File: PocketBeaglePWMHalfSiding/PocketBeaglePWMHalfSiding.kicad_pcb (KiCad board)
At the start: 2 copper layers, 149.9 x 128.3 mm, 61 parts, among them IC1 MCT6H, IC2 MCT6H, J1 RJ45, J2 RJ45, P1 POCKETBEAGLE-P1, P2 POCKETBEAGLE-P2, P3 C A0 A1 A2 A3 A4 A5 A6 A7, P4 C B0 B1 B2 B3 B4 B5 B6 B7, T1 + 15 in -, T2 + 15 out -, T3 In Track1 Out, T4 In Track1 Out, T5 Motor 1, T6 Motor 2, U1 TCAN332DR, U2 SN65HVD233-HT, U3 LM2574N-5.0, U4 PCA9685, U5 TBD62X83A, U6 TBD62X83A, U7 TC4428, U8 TC4428, U9 74HCT00

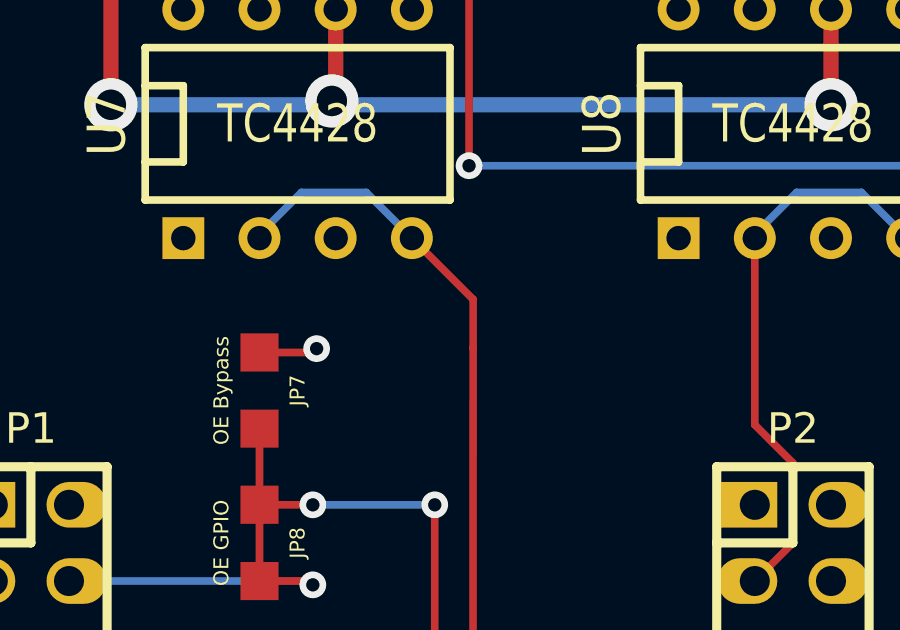
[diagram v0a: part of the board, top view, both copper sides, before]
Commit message: Mark orientation of ESP32 and PocketBeagle modules on the silk.
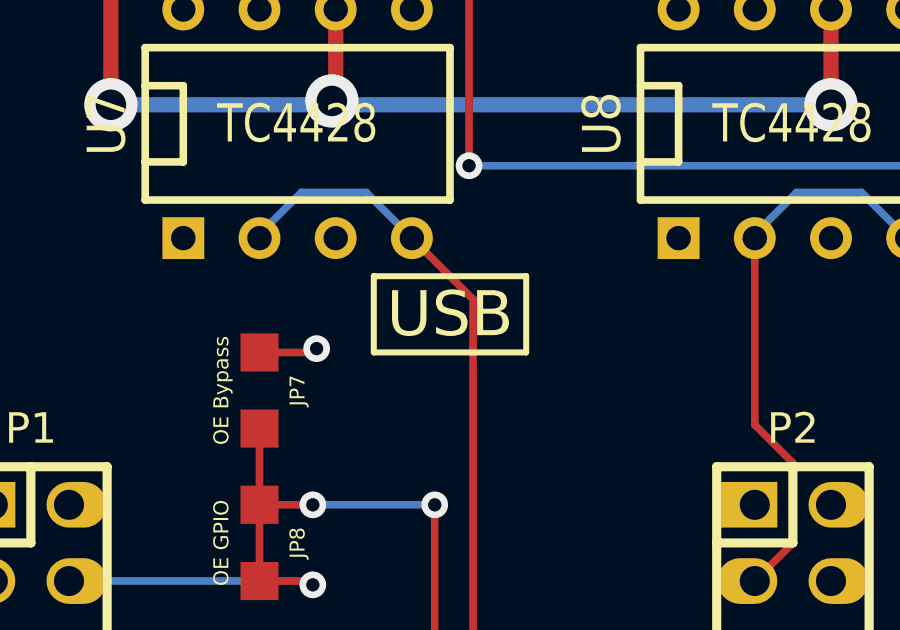
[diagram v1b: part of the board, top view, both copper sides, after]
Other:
- board text added: "USB"
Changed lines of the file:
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@@
     (area 38.269994 56.34548 243.868126 186.32358)
     (thickness 1.6)
-    (drawings 8)
+    (drawings 13)
     (tracks 644)
     (zones 0)
@@
     )
   )
+  (gr_line (start 144.78 73.66) (end 144.78 76.2) (angle 90) (layer F.SilkS) (width 0.2))
+  (gr_line (start 139.7 73.66) (end 144.78 73.66) (angle 90) (layer F.SilkS) (width 0.2))
+  (gr_line (start 139.7 76.2) (end 139.7 73.66) (angle 90) (layer F.SilkS) (width 0.2))
+  (gr_line (start 144.78 76.2) (end 139.7 76.2) (angle 90) (layer F.SilkS) (width 0.2))
+  (gr_text USB (at 142.24 74.93) (layer F.SilkS)
+    (effects (font (size 1.5 1.5) (thickness 0.3)))
+  )
   (gr_line (start 215.9 129.54) (end 163.83 129.54) (angle 90) (layer Edge.Cuts) (width 0.1))

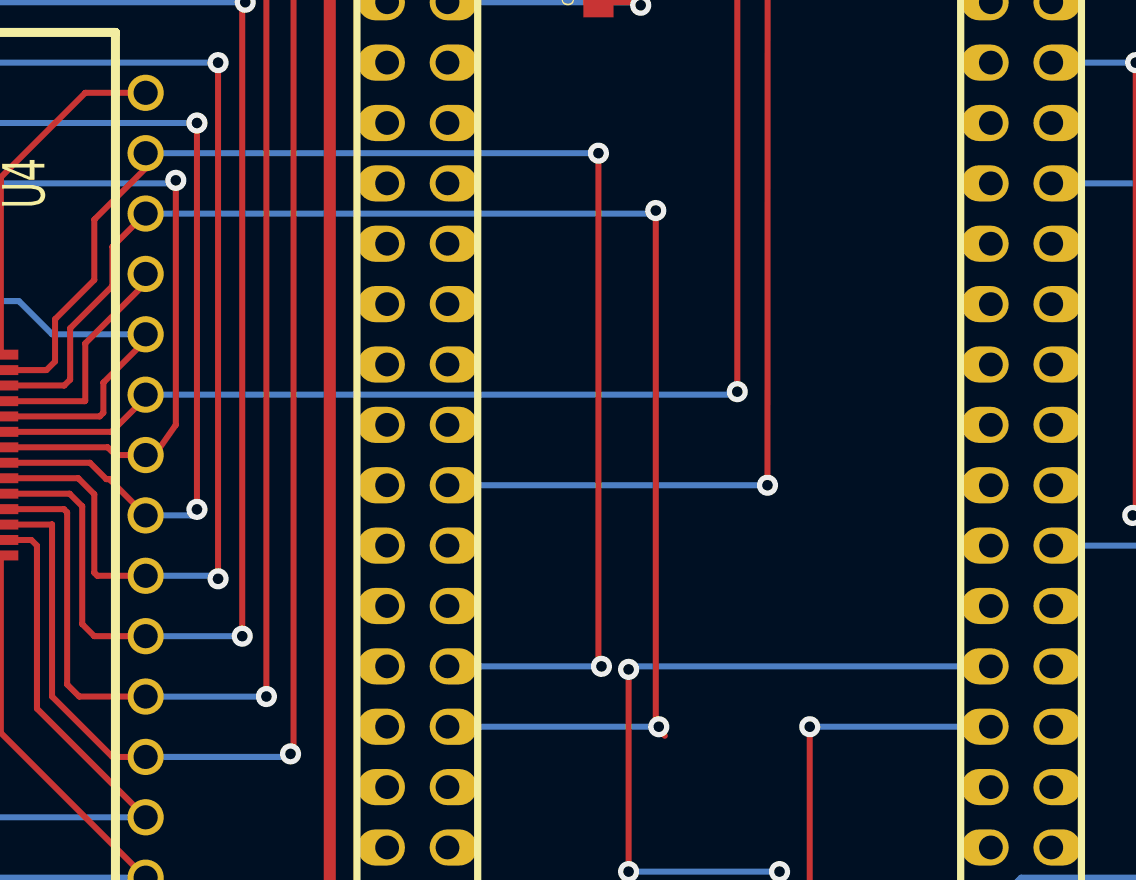
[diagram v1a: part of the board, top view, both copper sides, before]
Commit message: Move Pocket Beagle SDA usage from I2C2 to I2C1 (reserved I2C for eeprom?).
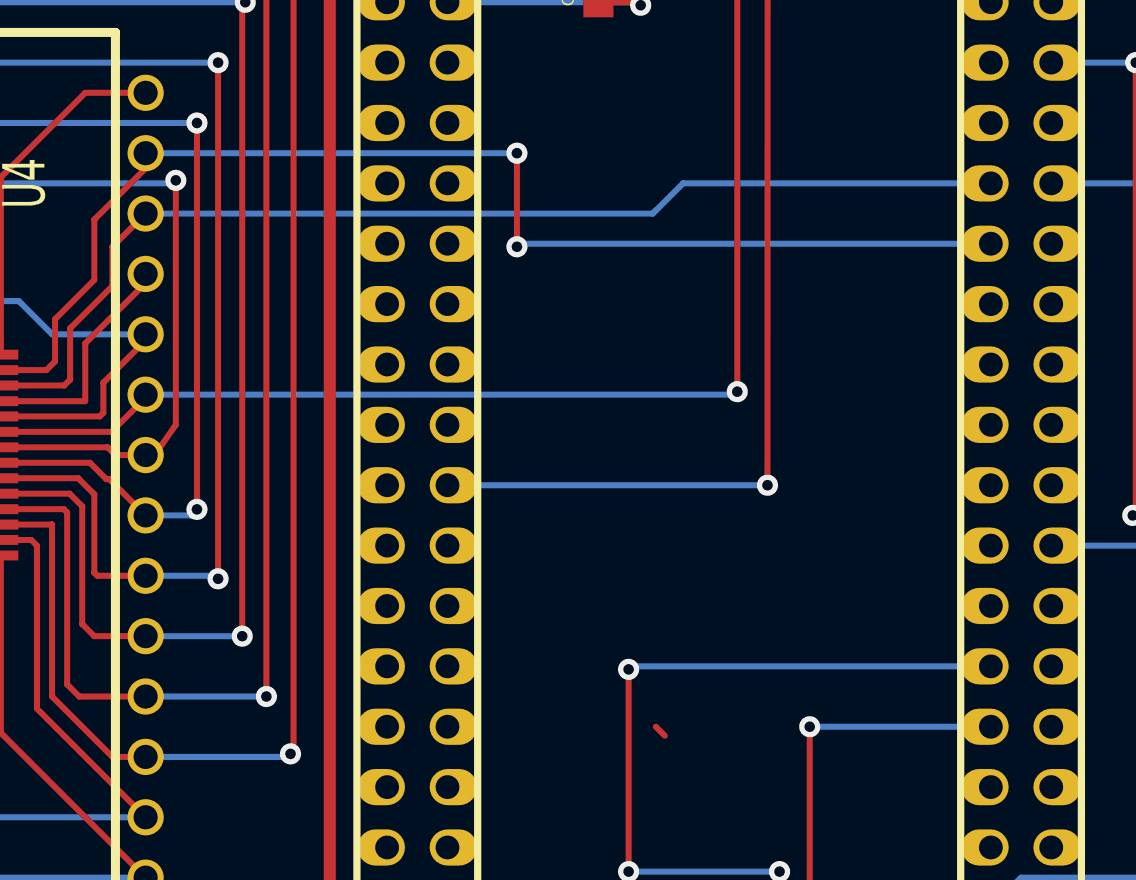
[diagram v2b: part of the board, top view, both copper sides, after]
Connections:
- P1 pad 26: /PCA9685 Driver/SDA -> (no net)
- P1 pad 28: /PCA9685 Driver/SCL -> (no net)
- P2 pad 11: (no net) -> /PCA9685 Driver/SDA
- P2 pad 9: (no net) -> /PCA9685 Driver/SCL
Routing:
- net /PCA9685 Driver/SCL: track 64.0 -> 47.4 mm, vias 2 -> 0
- net /PCA9685 Driver/SDA: track 59.9 -> 52.3 mm
- net (no net): track 0.00 -> 0.54 mm
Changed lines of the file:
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@@
     (thickness 1.6)
     (drawings 13)
-    (tracks 644)
+    (tracks 642)
     (zones 0)
     (modules 61)
@@
     (pad 26 thru_hole oval (at 8.89 -1.27 270) (size 1.524 1.99898) (drill 1.00076 (offset 0 -0.24892))
       (layers *.Cu *.Mask F.SilkS)
-      (net 11 "/PCA9685 Driver/SDA")
     )
     (pad 27 thru_hole oval (at 11.43 1.27 270) (size 1.524 1.99898) (drill 1.00076 (offset 0 0.24892))
@@
     (pad 28 thru_hole oval (at 11.43 -1.27 270) (size 1.524 1.99898) (drill 1.00076 (offset 0 -0.24892))
       (layers *.Cu *.Mask F.SilkS)
-      (net 10 "/PCA9685 Driver/SCL")
     )
     (pad 29 thru_hole oval (at 13.97 1.27 270) (size 1.524 1.99898) (drill 1.00076 (offset 0 0.24892))
@@
     (pad 9 thru_hole oval (at -11.43 1.27 270) (size 1.524 1.99898) (drill 1.00076 (offset 0 0.24892))
       (layers *.Cu *.Mask F.SilkS)
+      (net 10 "/PCA9685 Driver/SCL")
     )
     (pad 10 thru_hole oval (at -11.43 -1.27 270) (size 1.524 1.99898) (drill 1.00076 (offset 0 -0.24892))
@@
     (pad 11 thru_hole oval (at -8.89 1.27 270) (size 1.524 1.99898) (drill 1.00076 (offset 0 0.24892))
       (layers *.Cu *.Mask F.SilkS)
+      (net 11 "/PCA9685 Driver/SDA")
     )
     (pad 12 thru_hole oval (at -8.89 -1.27 270) (size 1.524 1.99898) (drill 1.00076 (offset 0 -0.24892))
@@
   (gr_line (start 118.11 185.42) (end 163.83 185.42) (angle 90) (layer Edge.Cuts) (width 0.1))
   (gr_line (start 118.11 129.54) (end 118.11 185.42) (angle 90) (layer Edge.Cuts) (width 0.1))
+  (segment (start 138.303 114.3) (end 138.684 114.681) (width 0.254) (layer F.Cu) (net 0))
   (segment (start 144.145 143.891) (end 144.145 147.828) (width 0.508) (layer F.Cu) (net 1))
   (segment (start 157.48 148.59) (end 160.02 151.13) (width 0.508) (layer B.Cu) (net 1))
@@
   (via (at 137.668 83.947) (size 0.889) (layers F.Cu B.Cu) (net 9))
   (segment (start 137.541 83.82) (end 137.668 83.947) (width 0.254) (layer F.Cu) (net 9))
-  (segment (start 138.303 92.583) (end 138.303 114.3) (width 0.254) (layer F.Cu) (net 10))
+  (segment (start 152.4 91.44) (end 139.446 91.44) (width 0.254) (layer B.Cu) (net 10))
+  (segment (start 139.446 91.44) (end 138.303 92.583) (width 0.254) (layer B.Cu) (net 10))
   (segment (start 138.176 92.71) (end 138.303 92.583) (width 0.254) (layer B.Cu) (net 10))
-  (via (at 138.303 92.583) (size 0.889) (layers F.Cu B.Cu) (net 10))
   (segment (start 116.84 92.71) (end 138.176 92.71) (width 0.254) (layer B.Cu) (net 10))
-  (segment (start 138.303 114.3) (end 138.684 114.681) (width 0.254) (layer F.Cu) (net 10))
-  (segment (start 138.43 114.3) (end 129.54 114.3) (width 0.254) (layer B.Cu) (net 10))
-  (via (at 138.43 114.3) (size 0.889) (layers F.Cu B.Cu) (net 10))
   (segment (start 110.74908 99.94392) (end 113.41608 99.94392) (width 0.254) (layer F.Cu) (net 10))
   (segment (start 115.443 94.107) (end 116.84 92.71) (width 0.254) (layer F.Cu) (net 10))
@@
   (segment (start 113.665 99.695) (end 113.665 97.536) (width 0.254) (layer F.Cu) (net 10))
   (segment (start 113.41608 99.94392) (end 113.665 99.695) (width 0.254) (layer F.Cu) (net 10))
-  (segment (start 129.54 111.76) (end 136.017 111.76) (width 0.254) (layer B.Cu) (net 11))
-  (segment (start 135.89 90.17) (end 116.84 90.17) (width 0.254) (layer B.Cu) (net 11))
-  (via (at 135.89 90.17) (size 0.889) (layers F.Cu B.Cu) (net 11))
-  (segment (start 135.89 111.633) (end 135.89 90.17) (width 0.254) (layer F.Cu) (net 11))
-  (segment (start 136.017 111.76) (end 135.89 111.633) (width 0.254) (layer F.Cu) (net 11))
-  (via (at 136.017 111.76) (size 0.889) (layers F.Cu B.Cu) (net 11))
+  (segment (start 152.4 93.98) (end 132.588 93.98) (width 0.254) (layer B.Cu) (net 11))
+  (segment (start 132.461 90.17) (end 116.84 90.17) (width 0.254) (layer B.Cu) (net 11))
+  (via (at 132.461 90.17) (size 0.889) (layers F.Cu B.Cu) (net 11))
+  (segment (start 132.461 94.107) (end 132.461 90.17) (width 0.254) (layer F.Cu) (net 11))
+  (via (at 132.461 94.107) (size 0.889) (layers F.Cu B.Cu) (net 11))
+  (segment (start 132.588 93.98) (end 132.461 94.107) (width 0.254) (layer B.Cu) (net 11))
   (segment (start 110.74908 99.29622) (end 112.66678 99.29622) (width 0.254) (layer F.Cu) (net 11))
   (segment (start 116.84 90.805) (end 116.84 90.17) (width 0.254) (layer F.Cu) (net 11))

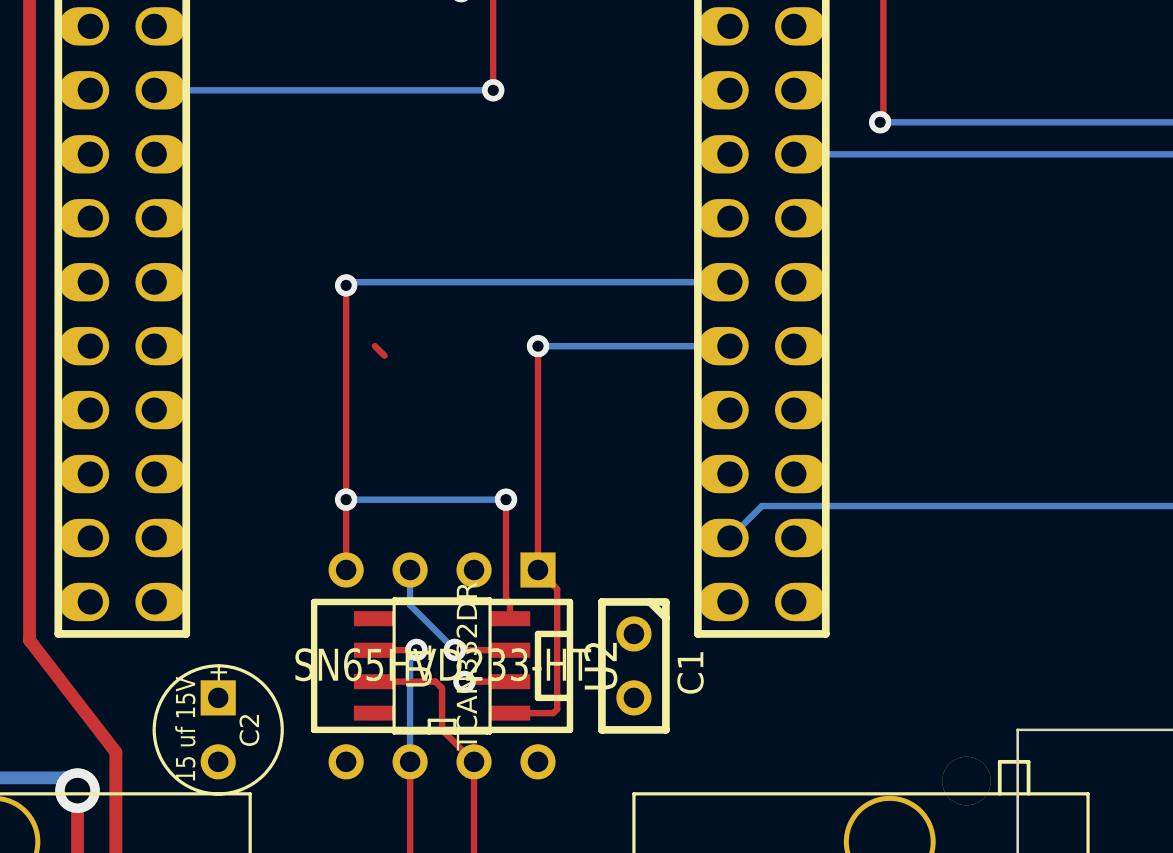
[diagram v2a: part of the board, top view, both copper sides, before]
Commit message: Add Console headers to all Pocket Beagle boards.
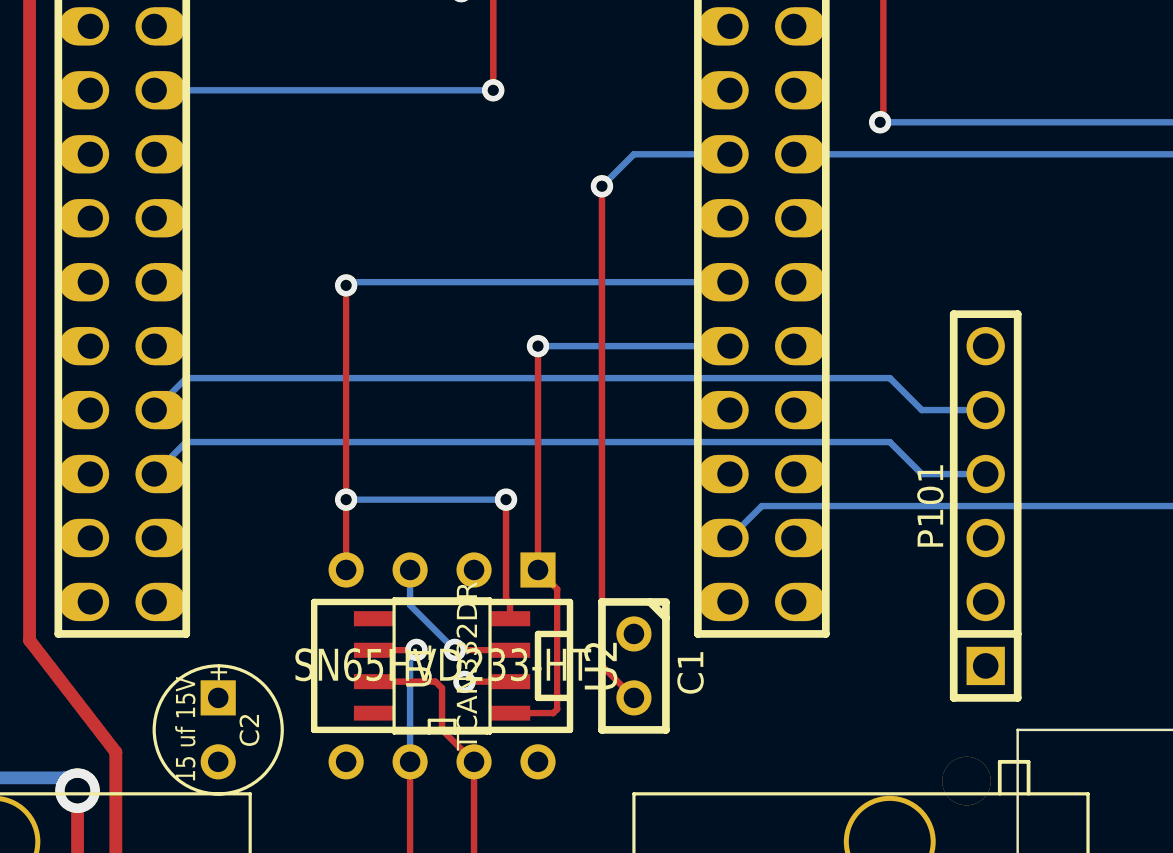
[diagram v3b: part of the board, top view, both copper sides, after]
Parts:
- added P101: Console, PIN_ARRAY-6X1, F.Cu at (162.6, 120.7)
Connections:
- P1 pad 30: (no net) -> N-000002
- P1 pad 32: (no net) -> N-000007
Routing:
- net N-000002: track 0.00 -> 34.1 mm
- net N-000007: track 0.00 -> 34.1 mm
- net GND: track 19.9 -> 46.3 mm, vias 2 -> 3
- net (no net): track 0.54 -> 0.00 mm
